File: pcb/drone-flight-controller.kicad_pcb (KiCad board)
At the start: 4 copper layers, 102 x 49 mm, 159 parts, among them J1 SWD, J10 CONN_MANDO, J11 OLED, J12 STM32 SPI, J13 STM32 I2C, J14 STM32 USART, J15 ICSP, J16 USB_B_Micro, J17 Conn_Coaxial, J2 Jumper, J3 USB_B_Micro, J4 CONN_MOT_1, J5 CONN_MOT_2, J6 CONN_MOT_3, J7 CONN_MOT_4, J8 XT-60, J9 LIDAR, SW1 TS-1088-AR02016_C720477, SW2 TS-1088-AR02016_C720477, SW3 TS-1088-AR02016_C720477, SW4 K3-1204D_C145861, U1 STM32F103R8T6, U10 LM7805_TO220, U11 AMS1117-3.3, U2 MPU-6050, U3 ATMEGA328P-AU, U4 CH340G, U5 LM358DR, U6 74HC245, U7 nRF24L01P, U8 MICROSD_C164170, U9 74AHC1G125, Y1 8MHz, Y2 32.768KHz, Y3 16MHz, Y4 12MHz, Y5 16MHz

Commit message: correct crystals ocs placement, copper zones and routing
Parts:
- moved C27 2.09 mm to (119.2, 82.5), turned to 90 degrees
- moved C44 2.00 mm to (117.5, 77.5)
- moved C43 2.00 mm to (117.1, 72.0)
- moved Y5 2.00 mm to (117.5, 74.7)
- moved C2 1.71 mm to (127.5, 108.0), turned to 180 degrees
- moved C34 1.18 mm to (115.0, 79.0)
- moved R37 0.99 mm to (115.0, 75.3)
- moved C22 0.90 mm to (111.1, 109.3)
- moved C20 0.87 mm to (111.1, 107.3)
- moved C11 0.84 mm to (118.8, 100.8)
- moved L3 0.82 mm to (111.7, 71.2)
- moved C12 0.79 mm to (118.8, 104.8)
- moved Y1 0.75 mm to (121.5, 102.8)
- moved L2 0.75 mm to (112.1, 73.0)
- moved L4 0.70 mm to (112.7, 71.5)
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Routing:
- net GND: track 0.00 -> 111.4 mm, vias 0 -> 106
- net +3.3V: track 0.00 -> 22.0 mm, vias 0 -> 16
- net /HSE_OUT: track 0.00 -> 10.9 mm
- net +5V: track 0.00 -> 10.3 mm, vias 0 -> 5
- net /HSE_IN: track 0.00 -> 8.94 mm
- net NRF_XC2: track 0.00 -> 7.31 mm
- net /LSE_IN: track 0.00 -> 6.84 mm
- net Net-(U4-XI): track 0.00 -> 6.64 mm
- net XTAL1_ATM328P: track 0.00 -> 6.08 mm
- net Net-(U4-XO): track 0.00 -> 5.90 mm
- net NRF_XC1: track 0.00 -> 5.49 mm
- net /LSE_OUT: track 0.10 -> 5.52 mm
- net XTAL2_ATM328P: track 0.00 -> 4.74 mm
- net Net-(U2-AD0): track 0.00 -> 3.64 mm
- net Net-(U7-IREF): track 0.00 -> 2.16 mm
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
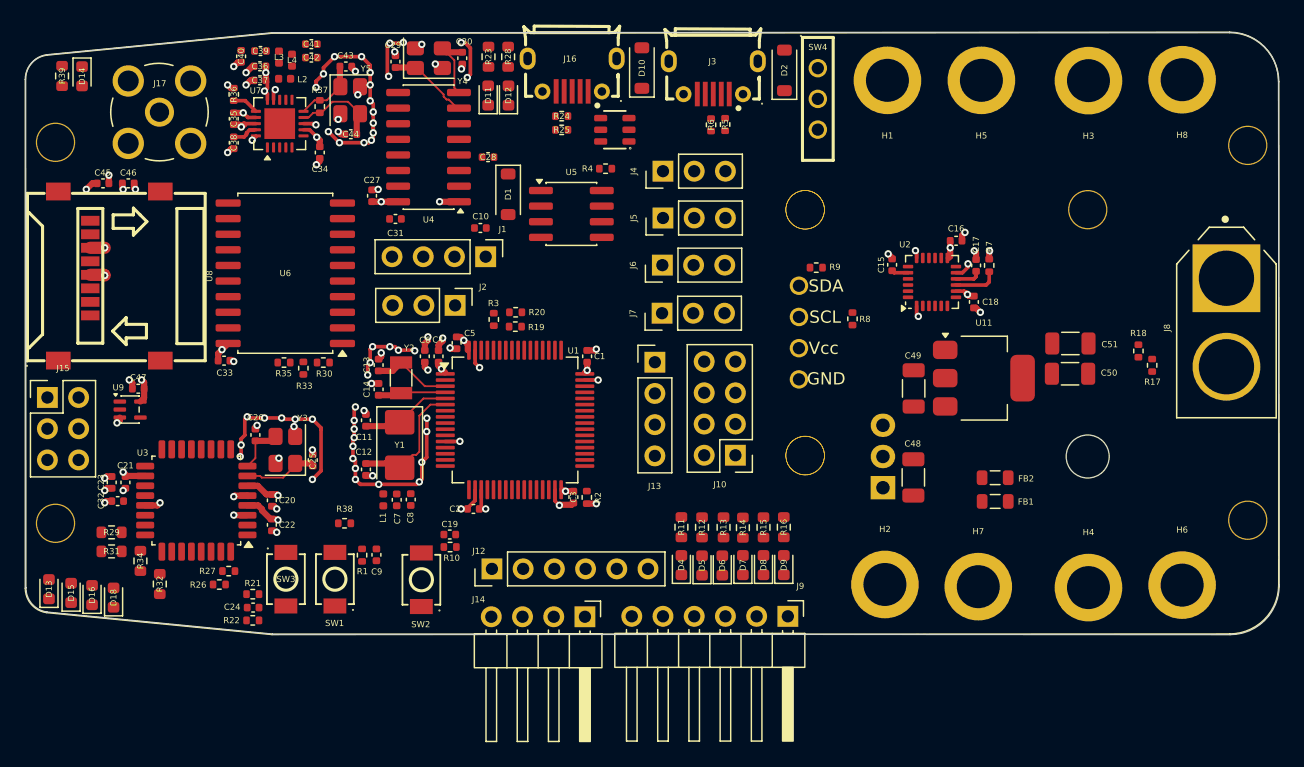
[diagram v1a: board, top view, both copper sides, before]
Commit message: finish drone controller pcb first pass
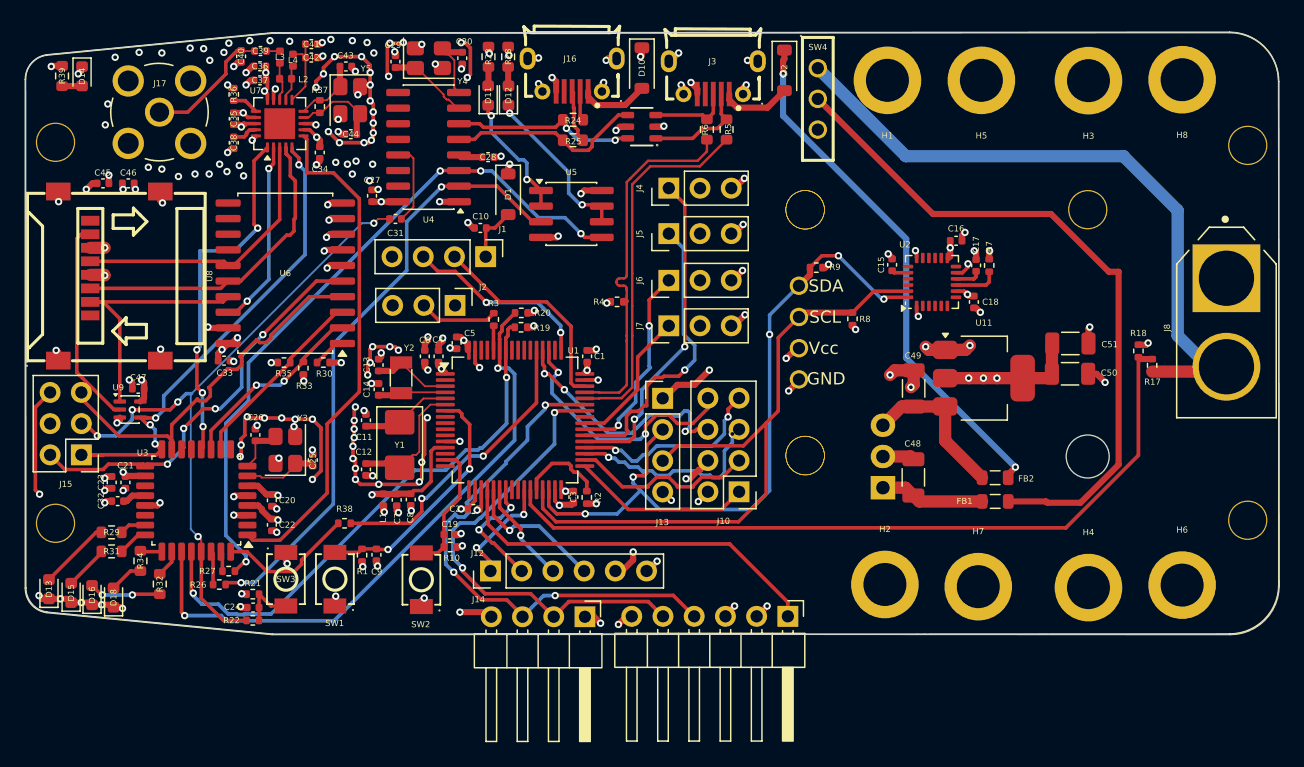
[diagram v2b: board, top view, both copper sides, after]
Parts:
- removed D4, D5, D6: ROJO, LED_SMD:LED_0603_1608Metric
- removed D7, D8: AZUL, LED_SMD:LED_0603_1608Metric
- removed D9: VERDE, LED_SMD:LED_0603_1608Metric
- removed R11, R12, R13: 750, Resistor_SMD:R_0603_1608Metric
- removed R14, R15: 220, Resistor_SMD:R_0603_1608Metric
- removed R16: 100, Resistor_SMD:R_0603_1608Metric
- added G***: LOGO, jpi-logos:jpi_logo_main, B.Cu at (113.8, 91.9)
- R24, R25, R5, R6: footprint Resistor_SMD:R_0402_1005Metric -> Resistor_SMD:R_0603_1608Metric
- moved R4 10.9 mm to (139.2, 91.2)
- moved J15 5.42 mm to (95.6, 103.6), turned to 180 degrees
- moved J13 3.00 mm to (142.9, 99.0)
- moved J10 2.99 mm to (149.1, 106.6)
- moved D3 2.21 mm to (141.2, 76.9)
- moved R5 1.53 mm to (146.5, 77.1), turned to -90 degrees
- moved J4 1.46 mm to (143.4, 81.9)
- moved J5 1.36 mm to (143.4, 85.6)
- moved J6 1.34 mm to (143.4, 89.4)
- moved R6 1.32 mm to (148.1, 77.1), turned to 90 degrees
- moved R25 1.25 mm to (135.6, 78.0)
- moved J7 1.16 mm to (143.4, 93.1)
- moved R24 0.97 mm to (135.6, 76.3)
- moved R19 0.47 mm to (131.4, 93.2)
- moved R20 0.47 mm to (131.4, 92.0)
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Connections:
- D3 pad 1: STM32_D+ -> STM32_D-
- D3 pad 3: STM32_D- -> STM32_D+
- D3 pad 4: ATM238P_D- -> ATM238P_D+
- D3 pad 6: ATM238P_D+ -> ATM238P_D-
- R26 pad 1: Net-(U4-TXD) -> RX_LED
- R27 pad 2: Net-(U4-RXD) -> TX_LED
- U1 pad 10: LED_3 -> unconnected-(U1-PC2-Pad10)
- U1 pad 11: LED_4 -> unconnected-(U1-PC3-Pad11)
- U1 pad 24: LED_5 -> unconnected-(U1-PC4-Pad24)
- U1 pad 25: LED_6 -> unconnected-(U1-PC5-Pad25)
- U1 pad 8: LED_1 -> unconnected-(U1-PC0-Pad8)
- U1 pad 9: LED_2 -> unconnected-(U1-PC1-Pad9)
- U4 pad 2: Net-(U4-TXD) -> RX_LED
- U4 pad 3: Net-(U4-RXD) -> TX_LED
- U5 pad 3: RX_ATM328P -> RX_LED
- U5 pad 5: TX_ATM328P -> TX_LED
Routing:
- net GND: track 111.4 -> 180.1 mm, vias 106 -> 193
- net ADC_Vbat: track 0.00 -> 63.1 mm
- net 12C2_SDA: track 0.00 -> 57.8 mm, vias 0 -> 5
- net TX_LED: track 0.00 -> 56.3 mm, vias 0 -> 4
- net +12C: track 0.00 -> 56.3 mm
- net 12C2_SCL: track 0.00 -> 56.0 mm
- net +12V: track 0.00 -> 55.5 mm
- net RST_ATM328P: track 0.00 -> 54.7 mm, vias 0 -> 5
- net 12C1_SDA: track 0.00 -> 50.4 mm, vias 0 -> 2
- net RX_LED: track 0.00 -> 50.2 mm, vias 0 -> 2
- net Vdrive: track 2.13 -> 50.9 mm, vias 1 -> 9
- net 12C1_SCL: track 0.00 -> 44.6 mm, vias 0 -> 2
- net USART1_RX: track 0.00 -> 43.9 mm, vias 0 -> 3
- net NRF_IRQ: track 0.00 -> 41.5 mm
- net MISO_ATM328P: track 0.00 -> 40.7 mm, vias 0 -> 4
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
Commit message: drc cleanup: board at 0 errors / 0 unconnected (was 40 errors + split 5V plane)
Reroute MISO_SD_OUT off J15.5 (real short), bridge the split +5V In2 plane
and drop sub-2mm2 islands, dedupe shared NPTH mounting holes so the fab
drills each location once, respace the ATmega USB pair to 0.2mm, pull fence
vias and edge silk clear of the outline, normalize silk text to the 0.8mm
minimum and relocate 58 refs. Remaining 91 warnings are structural
(In1-only GND fence vias), intentional (board-vs-lib divergence from the
NPTH dedupe), or dense-cluster refs needing hand placement.
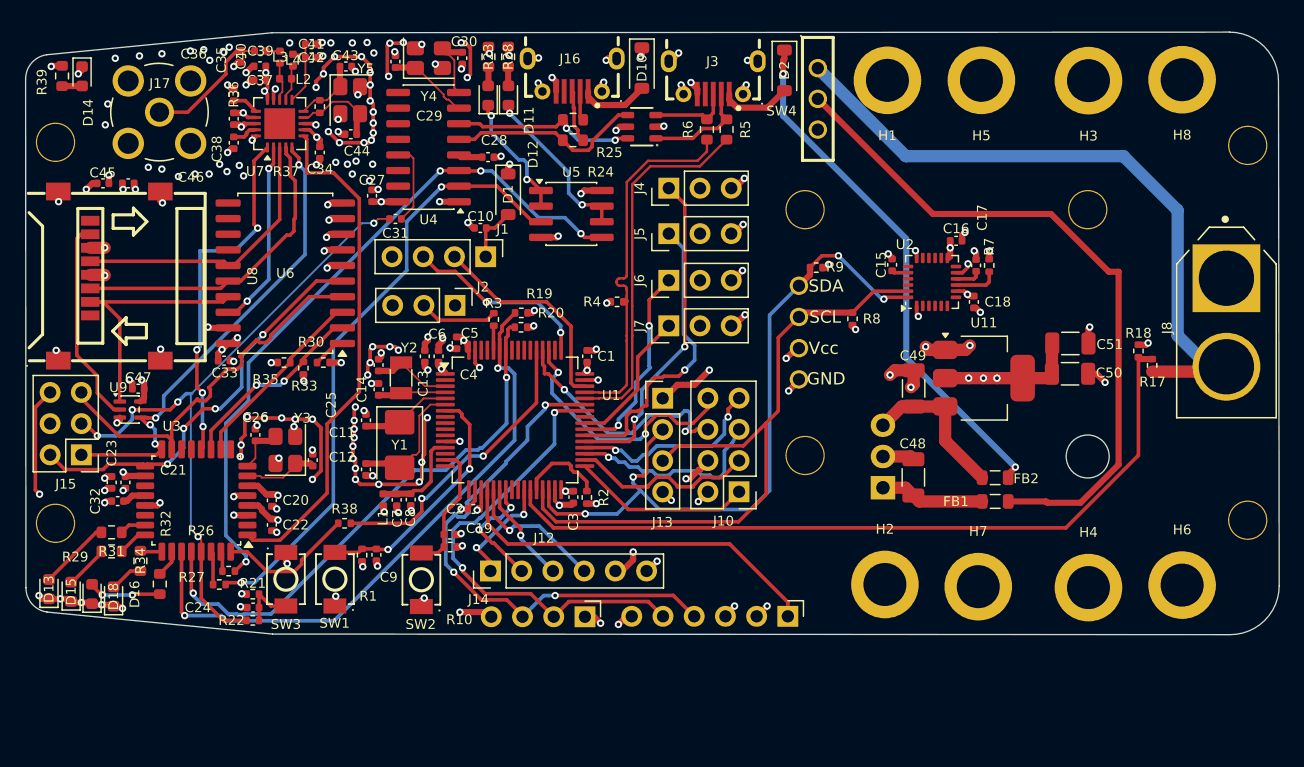
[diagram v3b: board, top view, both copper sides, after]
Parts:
- moved D15 0.09 mm to (94.8, 114.7)
- moved D16 0.09 mm to (96.5, 114.9)
- moved D18 0.09 mm to (98.2, 115.1)
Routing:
- net +5V: track 50.5 -> 56.4 mm
- net MISO_ATM328P: track 40.7 -> 39.0 mm
- net VDDA: track 8.99 -> 8.05 mm, vias 1 -> 0
- net MANDO_2: track 16.9 -> 17.8 mm, vias 2 -> 1
- net GND: track 180.1 -> 180.2 mm, vias 193 -> 191
- net MANDO_6: vias 3 -> 2
- net 12C2_SDA: vias 5 -> 4

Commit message: button references:
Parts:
- renumbered SW2 to INT, SW3 to RATM, SW1 to RSTM32
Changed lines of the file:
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@@
 		(layer "F.Cu")
 		(at 112.2426 113.7158 90)
-		(property "Reference" "SW3"
-			(at -3.67625 0 0)
+		(property "Reference" "RATM"
+			(at -3.67625 0.2574 0)
 			(layer "F.SilkS")
 			(effects
 				(font
-					(face "KiCad Font")
 					(size 0.8 0.8)
 					(thickness 0.15)
@@
 		(layer "F.Cu")
 		(at 116.2304 113.7158 -90)
-		(property "Reference" "SW1"
-			(at 3.5814 0.0254 180)
+		(property "Reference" "RSTM32"
+			(at 3.6842 -0.4696 180)
 			(layer "F.SilkS")
 			(effects
 				(font
-					(face "KiCad Font")
 					(size 0.8 0.8)
 					(thickness 0.15)
@@
 		(layer "F.Cu")
 		(at 123.2662 113.7622 -90)
-		(property "Reference" "SW2"
+		(property "Reference" "INT"
 			(at 3.6322 0.0508 0)
 			(layer "F.SilkS")
 			(effects
 				(font
-					(face "KiCad Font")
 					(size 0.8 0.8)
 					(thickness 0.15)

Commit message: texts and graphics
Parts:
- H1, H2, H3, H4: value M12V -> 12V
- H5, H6, H7, H8: value MGND -> GND
- moved G*** 13.8 mm to (127.5, 90.3)
- moved H5 0.17 mm to (168.8, 73.3)
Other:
- board text added: "12V"
- board text added: "GND"
- board text added: "https://github.com/A1DS19/drone-flight-controller"
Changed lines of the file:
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@@
 			)
 		)
+		(zone_connect 2)
 		(attr through_hole)
 		(duplicate_pad_numbers_are_jumpers no)
@@
 			)
 		)
+		(zone_connect 2)
 		(attr through_hole)
 		(duplicate_pad_numbers_are_jumpers no)
@@
 		(tags "Through hole pin header THT 1x03 2.54mm single row")
 		(property "Reference" "J2"
-			(at -1.4986 -2.2606 180)
+			(at -1.4986 -2.2606 0)
 			(layer "F.SilkS")
 			(effects
@@
 			)
 		)
+		(zone_connect 2)
 		(attr through_hole)
 		(duplicate_pad_numbers_are_jumpers no)
@@
 			)
 		)
+		(zone_connect 2)
 		(attr through_hole)
 		(duplicate_pad_numbers_are_jumpers no)
@@
 			(at 0 -4.5 0)
 			(layer "F.SilkS")
+			(hide yes)
 			(effects
 				(font
@@
 			)
 		)
-		(property "Value" "MGND"
-			(at 0 4.5 0)
-			(layer "F.Fab")
+		(property "Value" "GND"
+			(at -0.134 -4.5242 0)
+			(layer "F.SilkS")
 			(effects
 				(font
@@
 			)
 		)
+		(zone_connect 2)
 		(attr exclude_from_bom)
 		(duplicate_pad_numbers_are_jumpers no)
@@
 			(at 0 -4.5 0)
 			(layer "F.SilkS")
+			(hide yes)
 			(effects
 				(font
@@
 			)
 		)
-		(property "Value" "M12V"
-			(at 0 4.5 0)
-			(layer "F.Fab")
+		(property "Value" "12V"
+			(at -0.046 -4.3016 0)
+			(layer "F.SilkS")
 			(effects
 				(font
@@
 			(pinfunction "1_1")
 			(pintype "input")
+			(zone_connect 2)
 		)
 		(embedded_fonts no)
@@
 			(at 0 -4.5 0)
 			(layer "F.SilkS")
+			(hide yes)
 			(effects
 				(font
@@
 			)
 		)
-		(property "Value" "MGND"
-			(at 0 4.5 0)
-			(layer "F.Fab")
+		(property "Value" "GND"
+			(at 0.134 -4.5984 0)
+			(layer "F.SilkS")
 			(effects
 				(font
@@
 			)
 		)
+		(zone_connect 2)
 		(attr exclude_from_bom)
 		(duplicate_pad_numbers_are_jumpers no)
@@
 			)
 		)
+		(zone_connect 2)
 		(attr through_hole)
 		(duplicate_pad_numbers_are_jumpers no)
@@
 			(pinfunction "In_1")
 			(pintype "passive")
+			(zone_connect 2)
 		)
 		(pad "2" thru_hole circle
@@
 			(pinfunction "Ext_2")
 			(pintype "passive")
+			(zone_connect 2)
 		)
 		(pad "2" thru_hole circle
@@
 			(pinfunction "Ext_2")
 			(pintype "passive")
+			(zone_connect 2)
 		)
 		(pad "2" thru_hole circle
@@
 			(pinfunction "Ext_2")
 			(pintype "passive")
+			(zone_connect 2)
 		)
 		(pad "2" thru_hole circle
@@
 			(pinfunction "Ext_2")
 			(pintype "passive")
+			(zone_connect 2)
 		)
 		(embedded_fonts no)
@@
 			(at 0 -4.5 0)
 			(layer "F.SilkS")
+			(hide yes)
 			(effects
 				(font
@@
 			)
 		)
-		(property "Value" "M12V"
-			(at 0 4.5 0)
-			(layer "F.Fab")
+		(property "Value" "12V"
+			(at 0 -4.2476 0)
+			(layer "F.SilkS")
 			(effects
 				(font
@@
 			(pinfunction "1_1")
 			(pintype "input")
+			(zone_connect 2)
 		)
 		(embedded_fonts no)
@@
 			)
 		)
+		(zone_connect 2)
 		(attr through_hole)
 		(duplicate_pad_numbers_are_jumpers no)
@@
 			)
 		)
+		(zone_connect 2)
 		(attr through_hole)
 		(duplicate_pad_numbers_are_jumpers no)
@@
 			)
 		)
+		(zone_connect 2)
 		(attr through_hole)
 		(duplicate_pad_numbers_are_jumpers no)
@@
 			(at 0 -4.5 0)
 			(layer "F.SilkS")
+			(hide yes)
 			(effects
 				(font
@@
 			)
 		)
-		(property "Value" "MGND"
-			(at 0 4.5 0)
-			(layer "F.Fab")
+		(property "Value" "GND"
+			(at 0 -4.3254 0)
+			(layer "F.SilkS")
 			(effects
 				(font
@@
 			)
 		)
+		(zone_connect 2)
 		(attr exclude_from_bom)
 		(duplicate_pad_numbers_are_jumpers no)
@@
 		(tags "Through hole pin header THT 1x04 2.54mm single row")
 		(property "Reference" "J1"
-			(at -2.2352 -1.3716 180)
+			(at -2.2352 -1.3716 0)
 			(layer "F.SilkS")
 			(effects
@@
 			)
 		)
+		(zone_connect 2)
 		(attr through_hole)
 		(duplicate_pad_numbers_are_jumpers no)
@@
 	(footprint "easyeda:MountingHole_3.5mm_5.5mm"
 		(layer "F.Cu")
-		(at 168.8338 73.1266 180)
+		(at 168.8338 73.3 180)
 		(descr "Mounting Hole 3.5mm")
 		(tags "mounting hole 3.5mm")
@@
 			(at 0 -4.5 0)
 			(layer "F.SilkS")
+			(hide yes)
 			(effects
 				(font
@@
 			)
 		)
-		(property "Value" "MGND"
-			(at 0 4.5 0)
-			(layer "F.Fab")
+		(property "Value" "GND"
+			(at 0 -4.5 0)
+			(layer "F.SilkS")
 			(effects
 				(font
@@
 			)
 		)
+		(zone_connect 2)
 		(attr exclude_from_bom)
 		(duplicate_pad_numbers_are_jumpers no)
@@
 	(footprint "easyeda:MountingHole_3.5mm_5.5mm"
 		(layer "F.Cu")
-		(at 161.1884 73.1266 180)
+		(at 161.2 73.1 180)
 		(descr "Mounting Hole 3.5mm")
 		(tags "mounting hole 3.5mm")
@@
 			(at 0 -4.5 0)
 			(layer "F.SilkS")
+			(hide yes)
 			(effects
 				(font
@@
 			)
 		)
-		(property "Value" "M12V"
-			(at 0 4.5 0)
-			(layer "F.Fab")
+		(property "Value" "12V"
+			(at -0.1 -4.4 0)
+			(layer "F.SilkS")
 			(effects
 				(font
@@
 			)
 		)
+		(zone_connect 2)
 		(attr exclude_from_bom)
 		(duplicate_pad_numbers_are_jumpers no)
@@
 		(tags "Through hole angled pin header THT 1x04 2.54mm single row")
 		(property "Reference" "J14"
-			(at -1.4062 8.6614 180)
+			(at -1.4062 8.6614 0)
 			(layer "F.SilkS")
 			(effects
@@
 			)
 		)
+		(zone_connect 2)
 		(attr through_hole)
 		(duplicate_pad_numbers_are_jumpers no)
@@
 			(at 0 -4.5 0)
 			(layer "F.SilkS")
+			(hide yes)
 			(effects
 				(font
@@
 			)
 		)
-		(property "Value" "M12V"
-			(at 0 4.5 0)
-			(layer "F.Fab")
+		(property "Value" "12V"
+			(at 0 -4.448 0)
+			(layer "F.SilkS")
 			(effects
 				(font
@@
 			)
 		)
+		(zone_connect 2)
 		(attr exclude_from_bom)
 		(duplicate_pad_numbers_are_jumpers no)
@@
 			)
 		)
+		(zone_connect 2)
 		(attr through_hole)
 		(duplicate_pad_numbers_are_jumpers no)
@@
 	(footprint "jpi-logos:jpi_logo_main"
 		(layer "B.Cu")
-		(at 113.8 91.9 180)
+		(at 127.5 90.3 180)
 		(property "Reference" "G***"
 			(at 0 0 0)
@@
 		(layer "Edge.Cuts")
 	)
+	(gr_text "GND"
+		(at 183.9 89.7 90)
+		(layer "F.SilkS")
+		(effects
+			(font
+				(size 1 1)
+				(thickness 0.15)
+			)
+		)
+	)
+	(gr_text "12V"
+		(at 184.1 96.9 90)
+		(layer "F.SilkS")
+		(effects
+			(font
+				(size 1 1)
+				(thickness 0.15)
+			)
+		)
+	)
+	(gr_text "https://github.com/A1DS19/drone-flight-controller"
+		(at 157.2006 110.1598 0)
+		(layer "B.SilkS")
+		(effects
+			(font
+				(size 1.5 1.5)
+				(thickness 0.3)
+				(bold yes)
+			)
+			(justify left bottom mirror)
+		)
+	)
 	(segment
